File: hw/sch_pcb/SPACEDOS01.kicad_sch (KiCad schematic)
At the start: 53 parts, among them M1 HOLE, M10 BMI-S-204-F, M2 HOLE, M3 HOLE, M4 HOLE, M6 BMI-S-210-F, M8 BMI-S-204-F, M9 BMI-S-204-F, U1 OPA2314, U2 OPA2314, U3 ISL21080DIH312Z-TK 1V25, U4 TS7211, U5 TS5A4594

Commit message: update ustid
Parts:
- C1: UST_ID (none) -> 650b58f1462c6d9e7205463b
- C10, C11, C12, C13, C14, C16, C2, C20: UST_ID (none) -> 5c70984712875079b91f8b4c
- C15: UST_ID (none) -> 5c70984712875079b91f8b47
- C17, C3: UST_ID (none) -> 5e3ff8fc1287502a33bad7a3
- C18: UST_ID (none) -> 5c70984712875079b91f8b46
- C19: UST_ID (none) -> 5c70984812875079b91f8ba6
- C21, C23, C4, C6, C7, C8, C9: UST_ID (none) -> 5c70984712875079b91f8b53
- C24: UST_ID (none) -> 5c70984712875079b91f8b50
- C5: UST_ID (none) -> 5c70984712875079b91f8b9f
- M1, M2, M3, M4: now left out of the parts list
- M10, M8, M9: UST_ID (none) -> 5c72751c1287500b4e11301a
- M6: UST_ID (none) -> 5c70984312875079b91f873d
- R1: UST_ID (none) -> 5c70984512875079b91f896d
- R10, R8: UST_ID (none) -> 5c70984512875079b91f898c
- R11, R15, R19, R22, R9: UST_ID (none) -> 5c70984612875079b91f8995
- R12, R7: UST_ID (none) -> 5c70984612875079b91f899f
- R13: UST_ID (none) -> 5c70984612875079b91f8990
- R2, R3, R4, R5: UST_ID (none) -> 5c70984512875079b91f8986
- R6: UST_ID (none) -> 5c70984712875079b91f8aae
- U1, U2: UST_ID (none) -> 5c70984412875079b91f879b
- U3: UST_ID (none) -> 5c70984712875079b91f8b7a
- U4: UST_ID (none) -> 5c70984712875079b91f8b5b
- U5: UST_ID (none) -> 5c70984612875079b91f8a0d

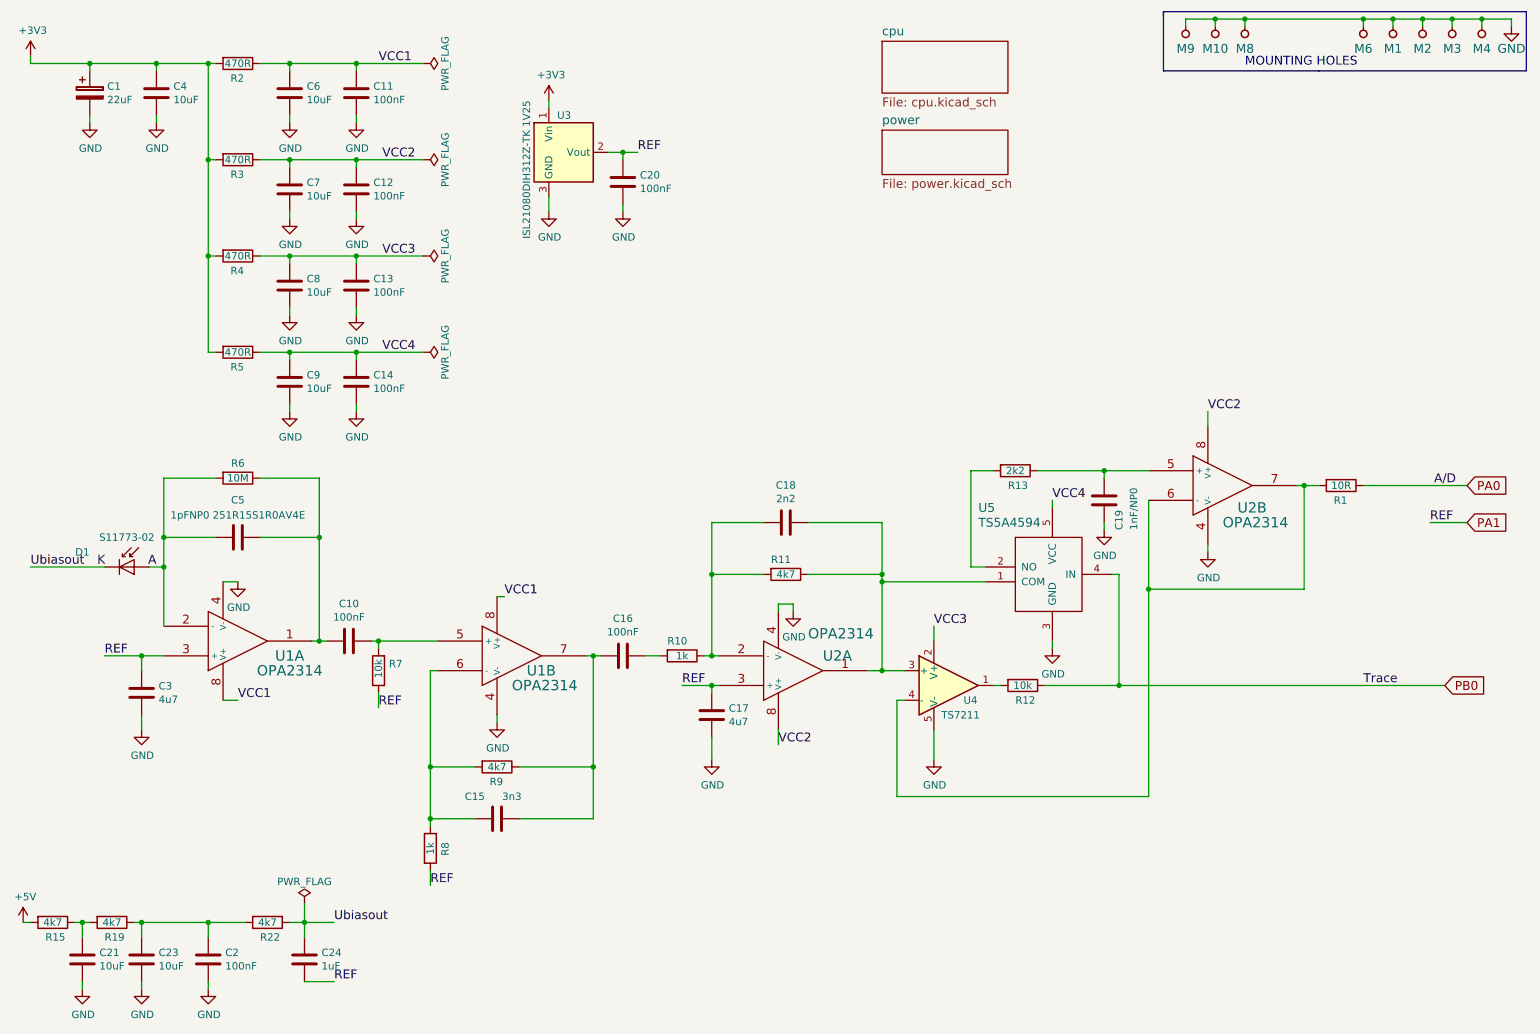
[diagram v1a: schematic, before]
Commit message: Update titleblock to fix schematics PDF generation. Improve schematics layout.
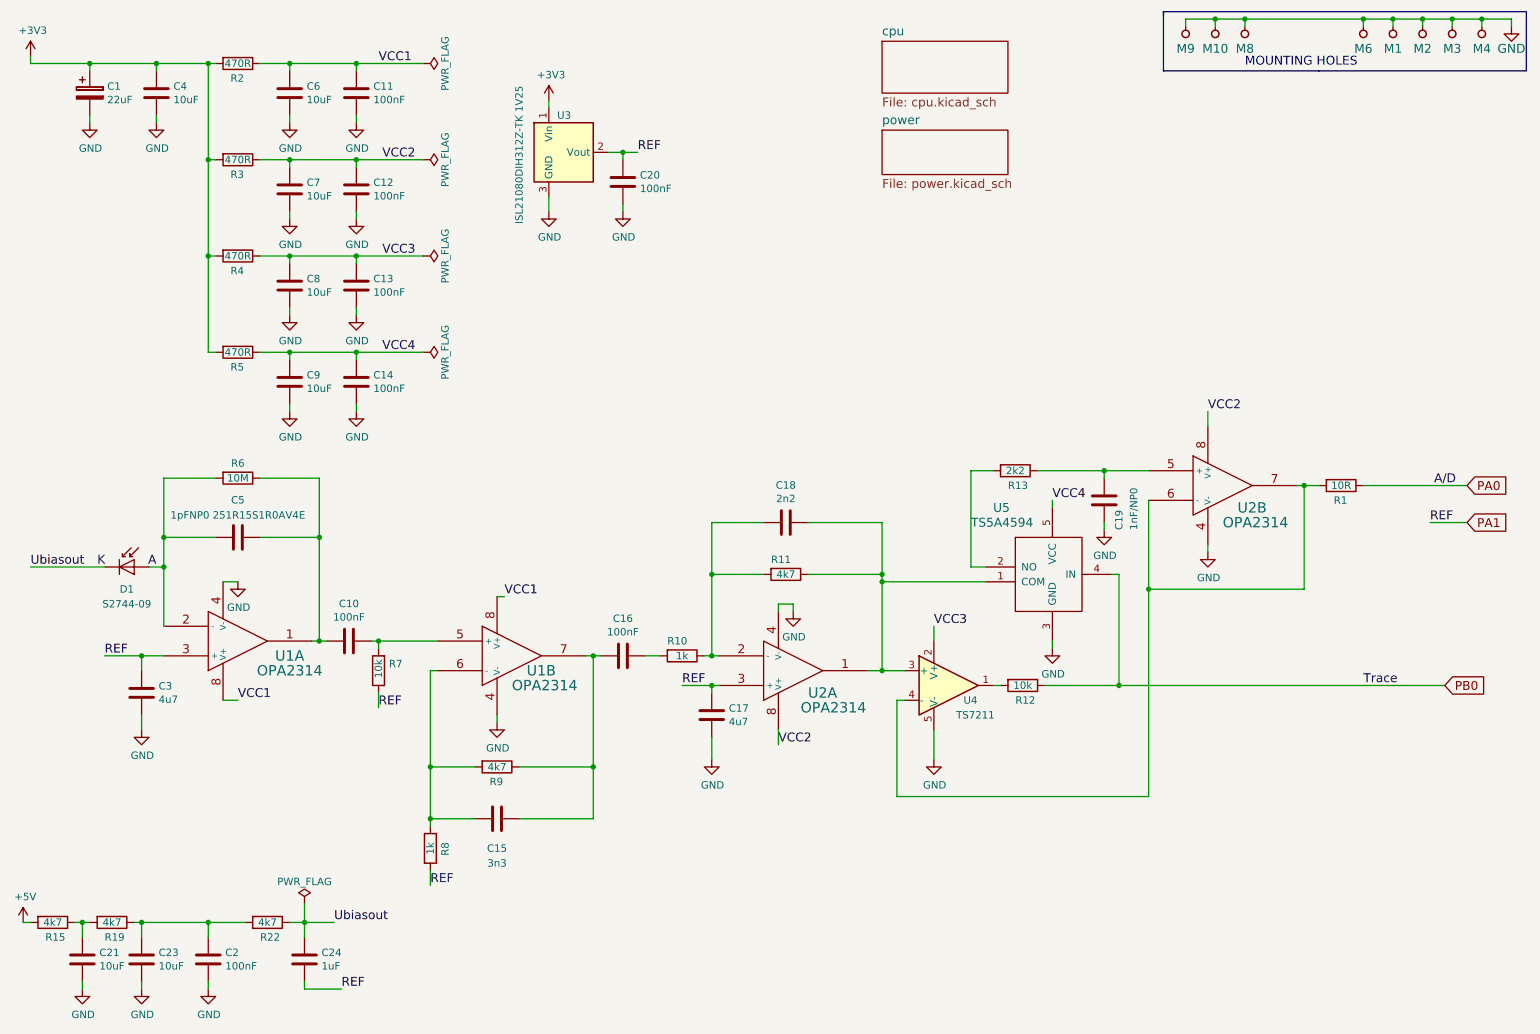
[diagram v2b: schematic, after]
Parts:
- D1: value S11773-02 -> S2744-09; UST_ID (none) -> 628d118cdc56076e9a2235e4

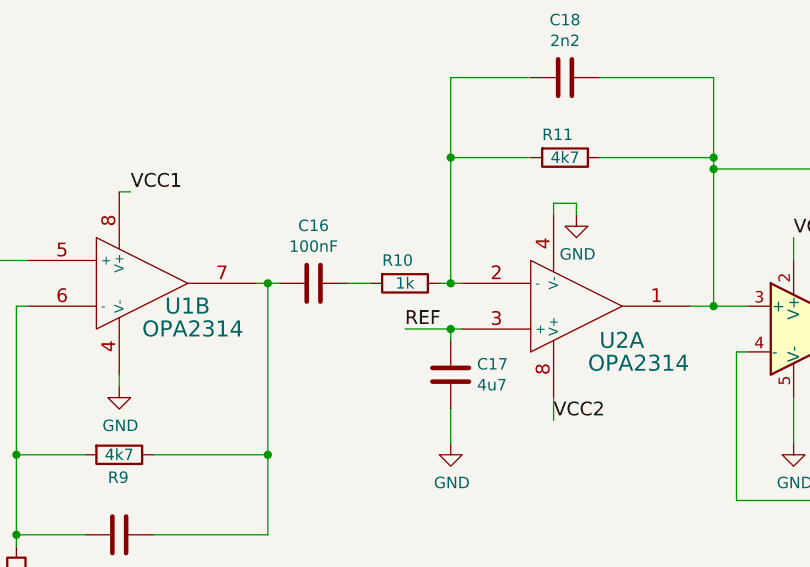
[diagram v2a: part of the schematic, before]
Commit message: Update project. Update components IDs
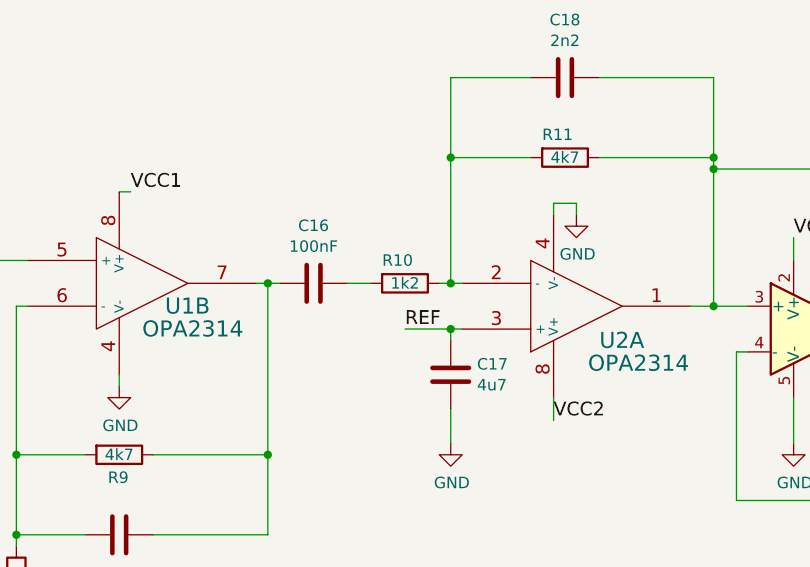
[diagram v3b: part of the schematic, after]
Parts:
- R10: value 1k -> 1k2; UST_ID 5c70984512875079b91f898c -> 5c70984512875079b91f898d
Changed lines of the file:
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@@
 			)
 		)
-		(property "Value" "1k"
+		(property "Value" "1k2"
 			(at 137.16 125.73 90)
 			(effects
@@
 			)
 		)
-		(property "UST_ID" "5c70984512875079b91f898c"
+		(property "UST_ID" "5c70984512875079b91f898d"
 			(at 137.16 125.73 90)
 			(effects
